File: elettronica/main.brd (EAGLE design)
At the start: 193 x 168.9 mm, 55 parts, among them IC1 74LS595D, IC3 7805TV, J2 2X6, J3 455-1750-1-ND

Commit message: continuare a posizionare i pezzi nella board
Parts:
- removed D2: 1N4148, diode:DO35-7
- removed J3: 455-1750-1-ND, SparkFun-Connectors:1X03
- removed R1: 10k, eagle-ltspice:R1206
- removed R2: 100, eagle-ltspice:R1206
- removed U$17: BNO055, BNO055:BNO005
- removed X2: (no value), con-ptr500:AK500/2-H
- moved R14 505.7 mm to (158.8, -36.8), turned to 270 degrees
- moved R13 478.0 mm to (121.9, -34.3), turned to 90 degrees
- moved D5 387.4 mm to (142.2, -43.2), turned to 180 degrees
- moved D4 380.8 mm to (142.2, -45.7)
- moved U$19 372.1 mm to (146.1, -29.2)
- moved X3 357.5 mm to (125.7, -59.7), turned to 180 degrees
- moved R5 355.6 mm to (57.1, -57.1)
- moved D9 355.4 mm to (30.5, -88.9), turned to 180 degrees
- moved R4 346.7 mm to (50.8, -53.3), turned to 180 degrees
- moved R3 344.0 mm to (57.1, -53.3)
- moved C10 342.7 mm to (130.8, -44.5), turned to 180 degrees
- moved X4 342.0 mm to (108.0, -73.7), turned to 90 degrees
- moved C9 339.3 mm to (130.8, -47.0), turned to 180 degrees
- moved C5 338.3 mm to (130.8, -49.5), turned to 180 degrees
- moved C6 335.1 mm to (130.8, -41.9), turned to 180 degrees
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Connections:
- removed net DRAIN: J3.2, X2.2
- new net N$2: D1.C, R3.2
- new net N$3: D3.C, R4.2
- new net N$6: D8.C, R7.2
- new net N$7: D9.C, R8.2
- new net N$8: D10.C, R9.2
- net 12V: no longer X2.1
- net 5V: no longer U$17.VIN
- net GND: no longer J3.3, R1.2, U$17.GND
- net KICK: no longer R2.2
- net LED1: no longer D1.C, R3.2
- net LED2: no longer D3.C, R4.2
- net LED3: no longer D6.C, R5.2
- net LED4: no longer D7.C, R6.2
- net LED5: no longer D8.C, R7.2
- net LED6: no longer D9.C, R8.2
- net LED7: no longer D10.C, R9.2
- net N$4: now also D6.C, R5.2; no longer D2.C, J3.1, R1.1
- net N$5: now also D7.C, R6.2; no longer D2.A, R2.1
- net SCL: no longer U$17.SCL
- net SDA: no longer U$17.SDA
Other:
- outline, holes or cut-outs redrawn

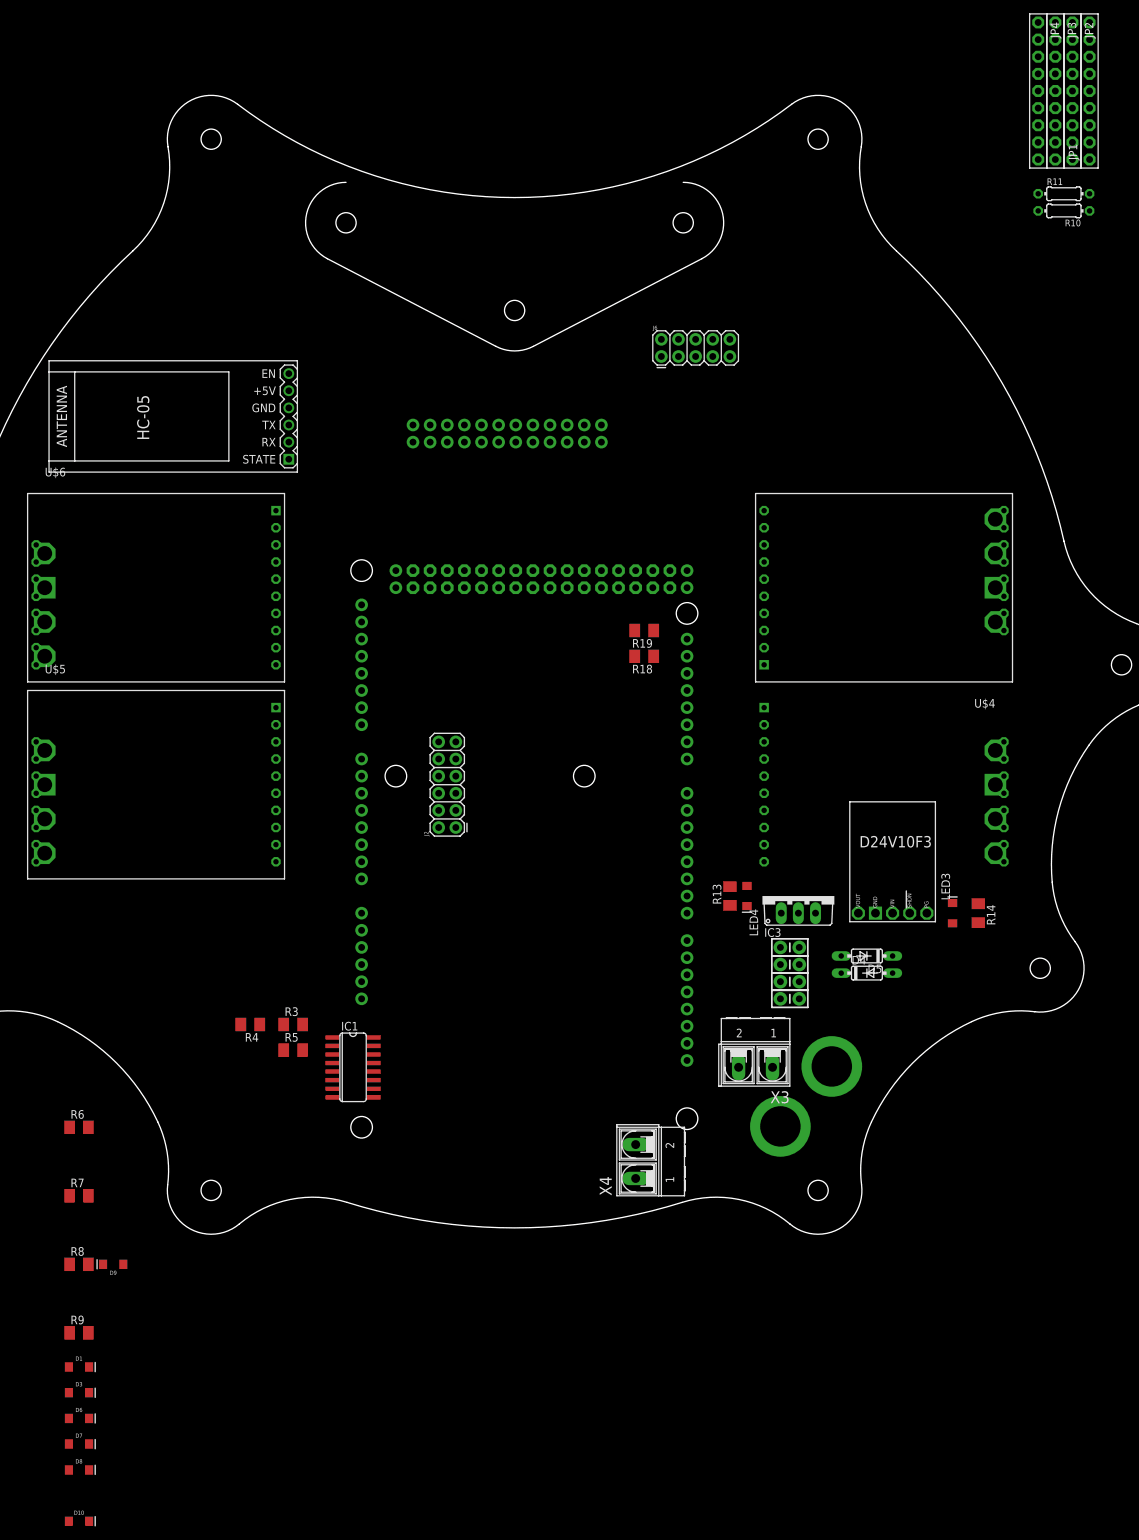
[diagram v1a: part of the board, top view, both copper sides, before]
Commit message: PCB Finita
posizionati tutti i componenti e tracciate tutte le piste
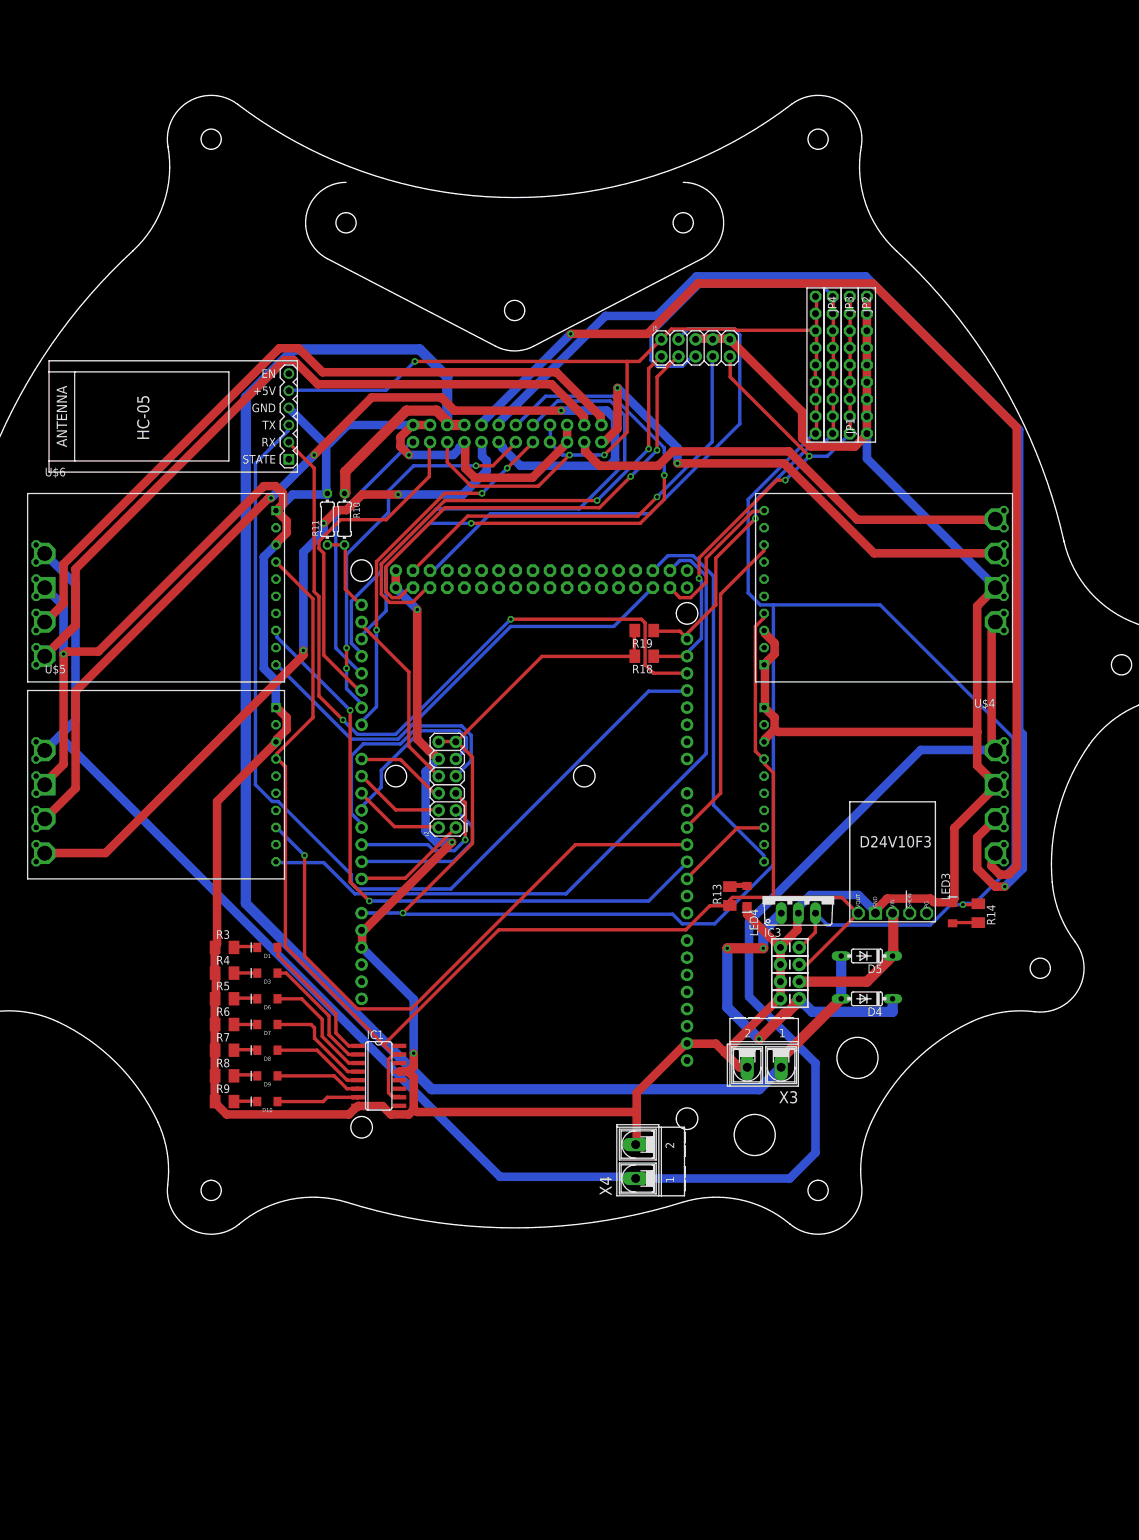
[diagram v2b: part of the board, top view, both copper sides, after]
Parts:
- removed U$3, U$8: DRILL_SWITCH, Switch drill:DRILL_SWITCH
- moved R11 119.4 mm to (62.2, 21.6), turned to 90 degrees
- moved R10 116.1 mm to (64.8, 21.6), turned to 270 degrees
- moved D1 68.2 mm to (53.3, -41.9), turned to 180 degrees
- moved D10 68.2 mm to (53.3, -64.8), turned to 180 degrees
- moved D3 68.2 mm to (53.3, -45.7), turned to 180 degrees
- moved D6 68.2 mm to (53.3, -49.5), turned to 180 degrees
- moved D7 68.2 mm to (53.3, -53.3), turned to 180 degrees
- moved D8 68.2 mm to (53.3, -57.1), turned to 180 degrees
- moved JP2 52.4 mm to (139.7, 44.5)
- moved JP3 52.4 mm to (137.2, 44.5)
- moved JP1 52.4 mm to (142.2, 44.5)
- moved JP4 52.4 mm to (134.6, 44.5)
- moved R9 40.5 mm to (47.0, -64.8)
- moved D9 36.1 mm to (53.3, -61.0)
- moved R8 35.3 mm to (47.0, -61.0)
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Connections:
- removed net N$22: B2.27
- removed net N$26: B2.28
- removed net N$27: B2.29
- removed net N$28: B2.30
- removed net N$29: B2.31
- removed net N$30: B2.32
- removed net N$31: B2.33
- removed net N$32: B2.34
- removed net N$33: B2.35
- new net 12VTO3.3: C9.1, D5.C, U$19.VIN
- new net 12VTO5: C5.1, D4.C, IC3.1
- net 12V: no longer C5.1, C9.1, D4.C, D5.C, IC3.1, U$19.VIN
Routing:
- net GND: track 0.00 -> 692.7 mm, vias 0 -> 6
- net 5V: track 0.00 -> 464.8 mm, vias 0 -> 6
- net VMOT: track 0.00 -> 279.1 mm
- net 12V: track 0.00 -> 255.1 mm
- net 3.3V: track 0.00 -> 230.4 mm
- net ROLLERA: track 0.00 -> 178.7 mm, vias 0 -> 1
- net ROLLERB: track 0.00 -> 169.2 mm, vias 0 -> 1
- net MOTA2: track 0.00 -> 145.5 mm, vias 0 -> 3
- net TX1: track 0.00 -> 138.9 mm
- net RX1: track 0.00 -> 110.5 mm, vias 0 -> 2
- net SCL: track 0.00 -> 109.0 mm, vias 0 -> 1
- net MOTA3: track 0.00 -> 108.2 mm
- net MOTB3: track 0.00 -> 107.8 mm
- net INA2: track 0.00 -> 107.7 mm
- net MOTB2: track 0.00 -> 103.3 mm, vias 0 -> 3
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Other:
- outline, holes or cut-outs redrawn

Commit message: pcb definitiva 2.0
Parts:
- added J1: (no value), SparkFun-Connectors:1X03
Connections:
- net GND: now also J1.1
- net KICK: now also J1.3
- net VMOT: now also J1.2
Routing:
- net KICK: track 0.00 -> 52.2 mm, vias 0 -> 2
- net VMOT: track 279.1 -> 299.2 mm
- net GND: track 692.7 -> 703.2 mm, vias 6 -> 5
- net SCL: track 109.0 -> 110.6 mm
- net 5V: track 464.8 -> 465.7 mm, vias 6 -> 5
- net SDA: track 90.8 -> 91.6 mm
- net 12VTO5: vias 4 -> 3

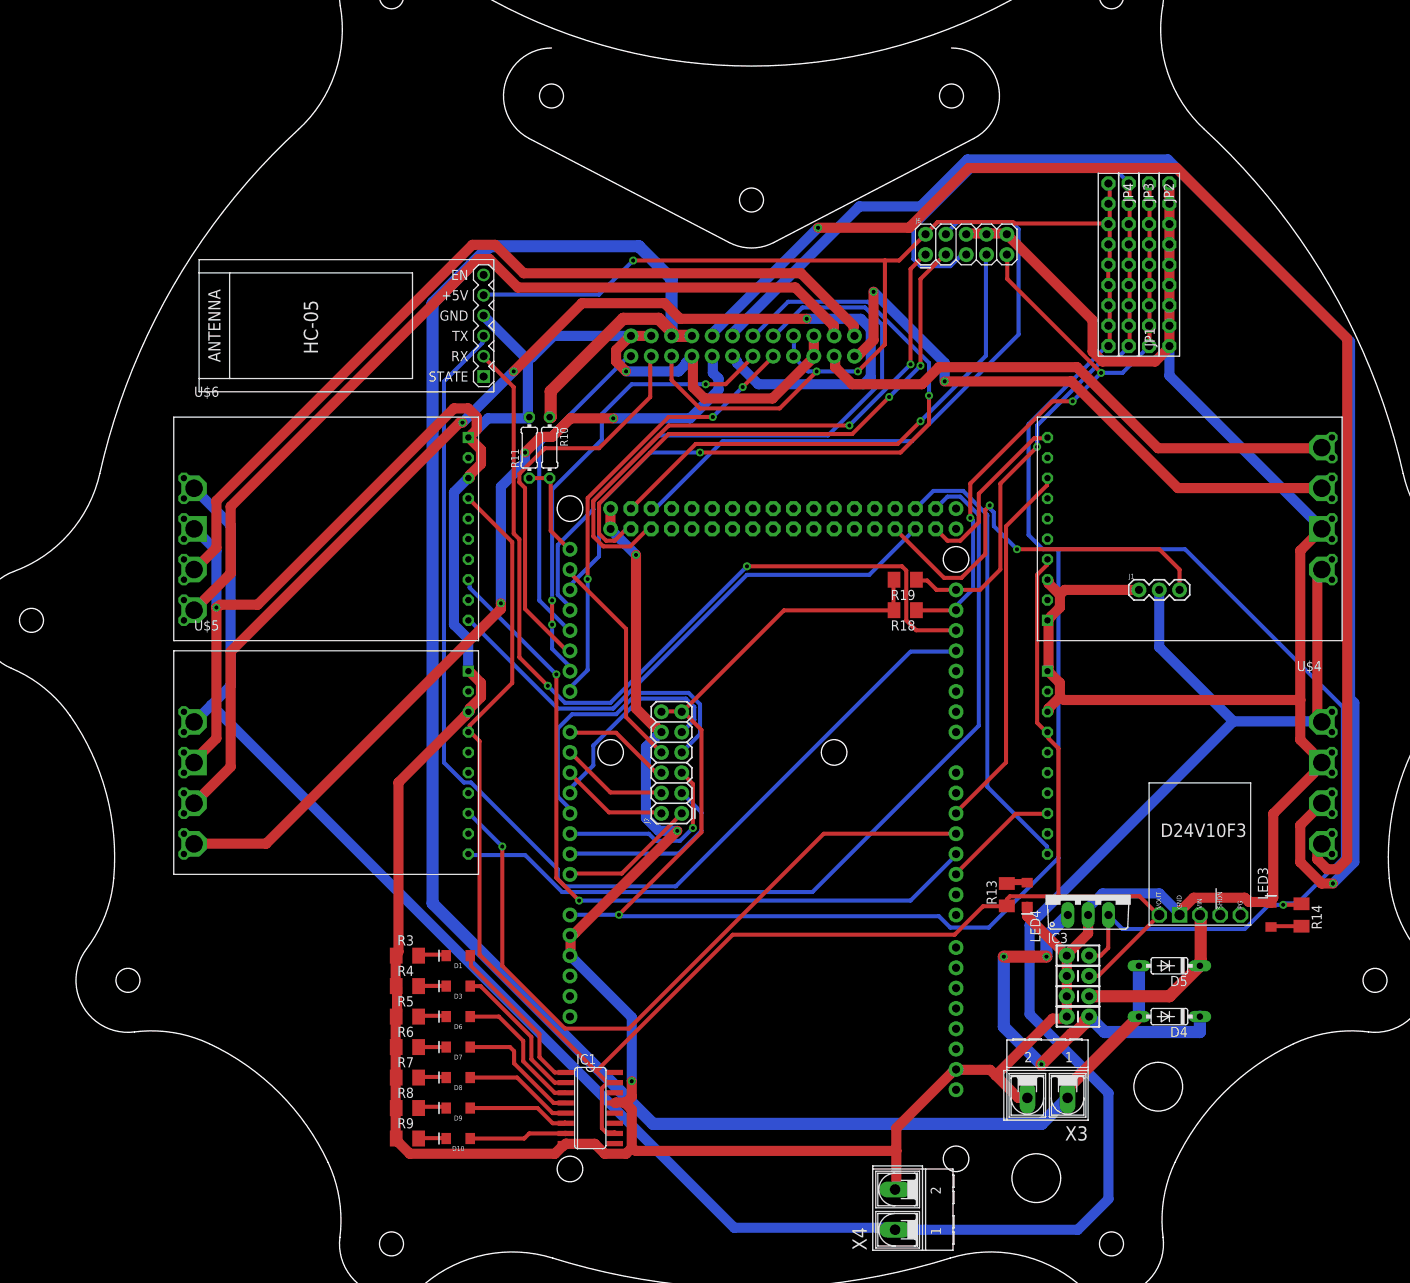
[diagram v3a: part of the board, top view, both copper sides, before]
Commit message: adding vector graphic
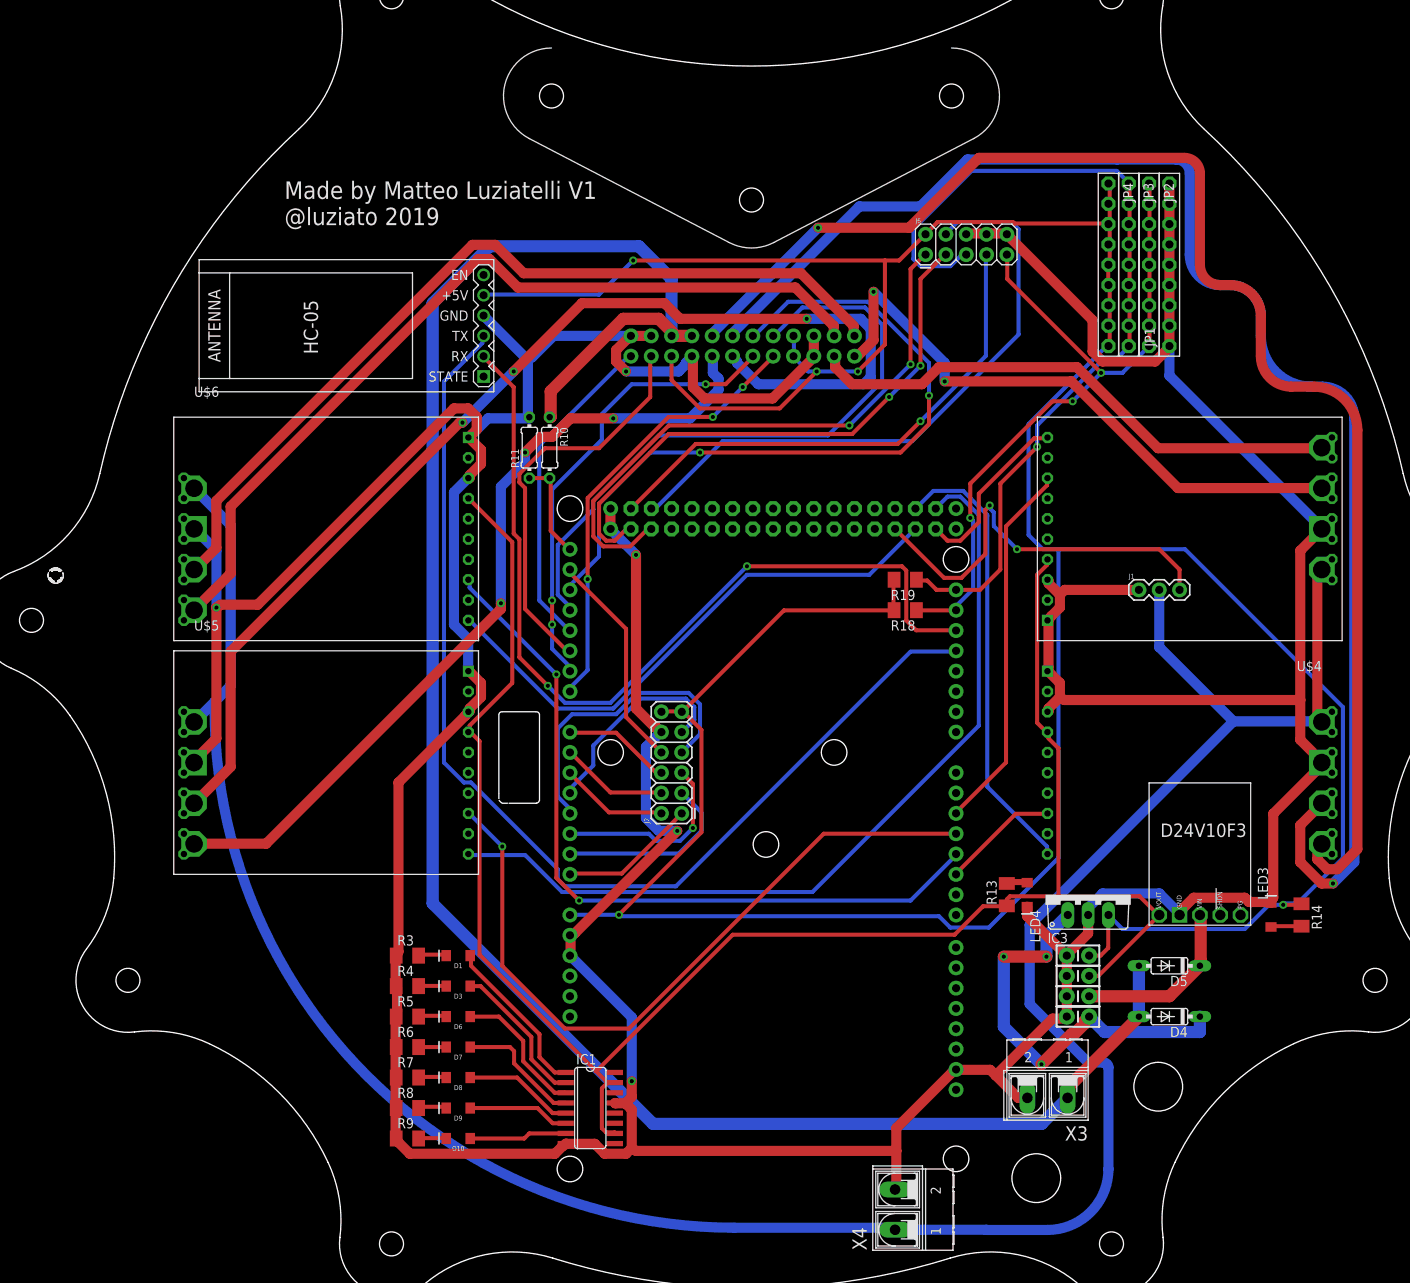
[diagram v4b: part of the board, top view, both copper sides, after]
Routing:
- net ROLLERB: track 169.2 -> 175.0 mm
- net ROLLERA: track 178.7 -> 180.8 mm
- net VMOT: track 299.2 -> 298.4 mm
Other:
- outline, holes or cut-outs redrawn
- board text added: "Made by Matteo Luziatelli V1 @luziato 2019"
